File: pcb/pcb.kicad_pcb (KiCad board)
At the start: 2 copper layers, 60 x 52 mm, 18 parts

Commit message: Improve board layout symmetry
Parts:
- moved J_LED_A 0.50 mm to (145.5, 103.0)
- turned J_LED_C to 270 degrees
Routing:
- net WIRE_B: track 121.7 -> 121.2 mm
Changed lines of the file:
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@@
 	(footprint "TerminalBlock_Phoenix:TerminalBlock_Phoenix_MKDS-1,5-2-5.08_1x02_P5.08mm_Horizontal"
 		(layer "F.Cu")
-		(at 145.5 102.5 90)
+		(at 145.5 103 90)
 		(property "Reference" "J_LED_A"
 			(at 0 0 0)
@@
 		)
 		(pad "1" thru_hole roundrect
-			(at 0 2.54 90)
+			(at 0 -2.54 90)
 			(size 2.8 2.8)
 			(drill 1.3)
@@
 		)
 		(pad "2" thru_hole circle
-			(at 0 -2.54 90)
+			(at 0 2.54 90)
 			(size 2.8 2.8)
 			(drill 1.3)
@@
 	(footprint "TerminalBlock_Phoenix:TerminalBlock_Phoenix_MKDS-1,5-2-5.08_1x02_P5.08mm_Horizontal"
 		(layer "F.Cu")
-		(at 145.5 142 90)
+		(at 145.5 142 270)
 		(property "Reference" "J_LED_C"
 			(at 0 0 0)
@@
 		)
 		(property "Datasheet" ""
-			(at 0 0 90)
+			(at 0 0 270)
 			(layer "F.Fab")
 			(hide yes)
@@
 		)
 		(property "Description" ""
-			(at 0 0 90)
+			(at 0 0 270)
 			(layer "F.Fab")
 			(hide yes)
@@
 		)
 		(pad "1" thru_hole roundrect
-			(at 0 2.54 90)
+			(at 0 2.54 270)
 			(size 2.8 2.8)
 			(drill 1.3)
@@
 		)
 		(pad "2" thru_hole circle
-			(at 0 -2.54 90)
+			(at 0 -2.54 270)
 			(size 2.8 2.8)
 			(drill 1.3)
@@
 	)
 	(gr_text "-"
-		(at 148.04 98.5 0)
+		(at 148.04 97 0)
 		(layer "F.SilkS")
 		(effects
@@
 			(polygon
 				(pts
-					(xy 147.789639 98.608154) (xy 147.789639 98.391609) (xy 148.291552 98.391609) (xy 148.291552 98.608154)
+					(xy 147.789639 97.108154) (xy 147.789639 96.891609) (xy 148.291552 96.891609) (xy 148.291552 97.108154)
 				)
 			)
@@
 	)
 	(gr_text "+"
-		(at 142.96 98.5 0)
+		(at 142.96 97 0)
 		(layer "F.SilkS")
 		(effects
@@
 			(polygon
 				(pts
-					(xy 142.852283 98.949881) (xy 142.852283 98.599978) (xy 142.536037 98.599978) (xy 142.536037 98.400261)
-					(xy 142.852283 98.400261) (xy 142.852283 98.050756) (xy 143.068431 98.050756) (xy 143.068431 98.400261)
-					(xy 143.384201 98.400261) (xy 143.384201 98.599978) (xy 143.068431 98.599978) (xy 143.068431 98.949881)
+					(xy 142.852283 97.449881) (xy 142.852283 97.099978) (xy 142.536037 97.099978) (xy 142.536037 96.900261)
+					(xy 142.852283 96.900261) (xy 142.852283 96.550756) (xy 143.068431 96.550756) (xy 143.068431 96.900261)
+					(xy 143.384201 96.900261) (xy 143.384201 97.099978) (xy 143.068431 97.099978) (xy 143.068431 97.449881)
 				)
 			)
@@
 	(segment
 		(start 148.04 107.5)
-		(end 148.04 102.5)
+		(end 148.04 103)
 		(width 1.6)
 		(layer "B.Cu")
@@
 	(segment
 		(start 140.96 104.5)
-		(end 142.96 102.5)
+		(end 142.96 103)
 		(width 1.8)
 		(layer "F.Cu")

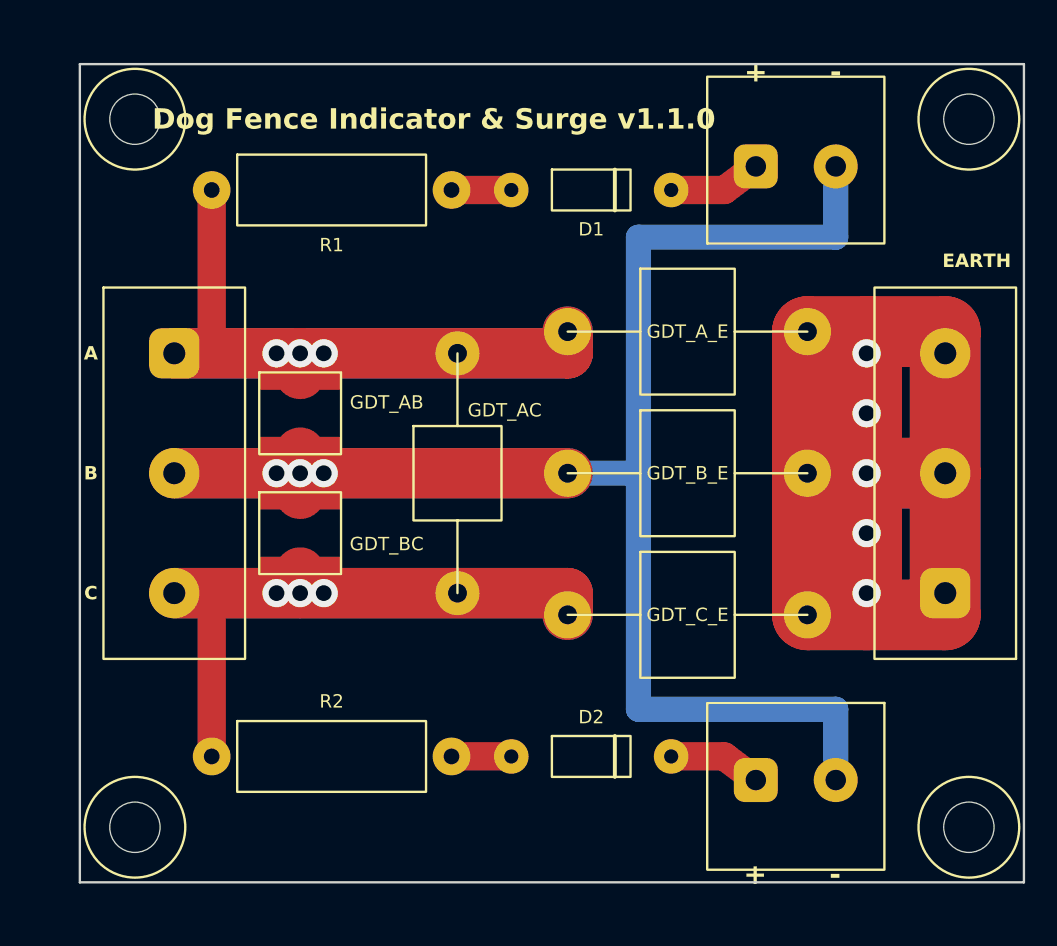
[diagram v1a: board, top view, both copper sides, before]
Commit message: Widen the board and shift components for clearer legibility of guide marks
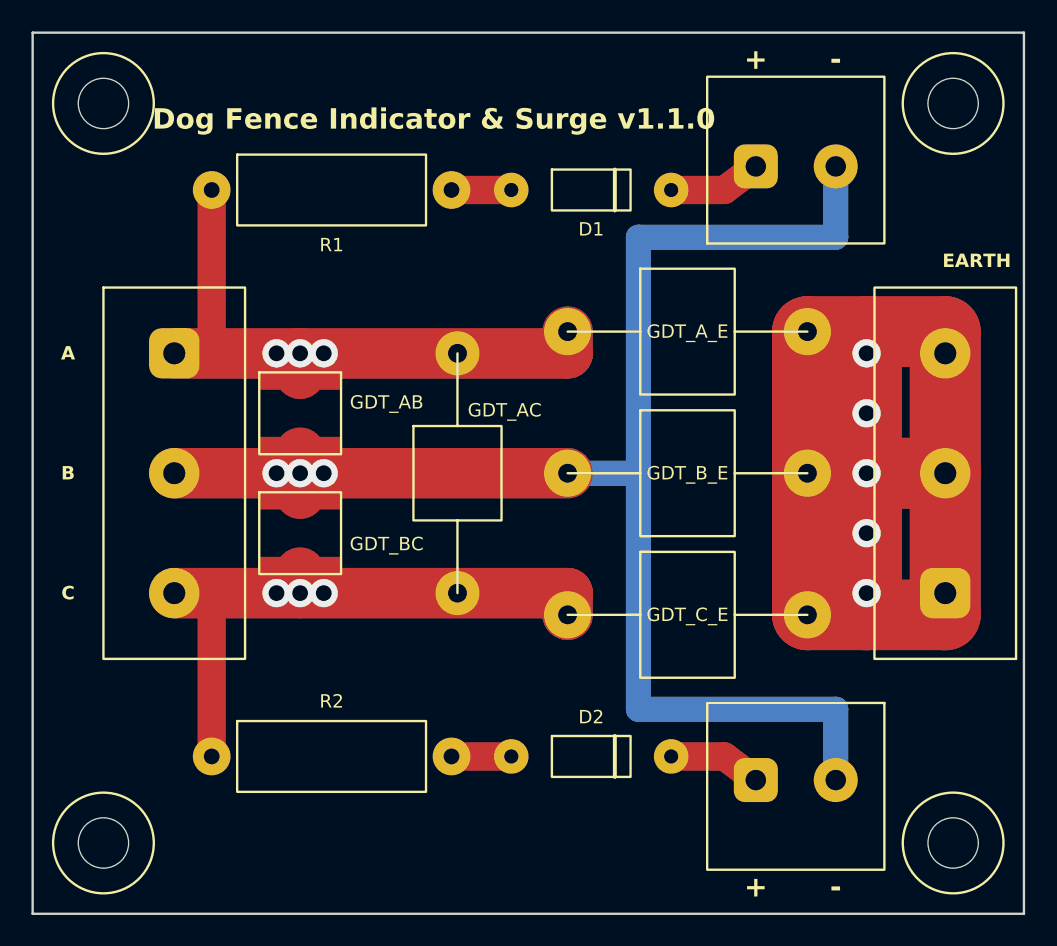
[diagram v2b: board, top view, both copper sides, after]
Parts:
- moved H1 2.24 mm to (101.5, 99.0)
- moved H3 2.24 mm to (101.5, 146.0)
- moved H2 1.41 mm to (155.5, 99.0)
- moved H4 1.41 mm to (155.5, 146.0)
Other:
- board size 60 x 52 mm -> 63 x 56 mm

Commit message: Review component assignments in light of JLCPCB stock availability
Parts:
- GDT_AC: value 2RA470-L5.5 -> B5G470L
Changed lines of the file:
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@@
 			)
 		)
-		(property "Value" "2RA470-L5.5"
+		(property "Value" "B5G470L"
 			(at 0 0 0)
 			(layer "F.Fab")
